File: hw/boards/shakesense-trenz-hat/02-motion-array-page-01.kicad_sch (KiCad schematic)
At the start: 12 parts, among them U11 LSM6DSOTR, U12 LSM6DSOTR, U13 LSM6DSOTR

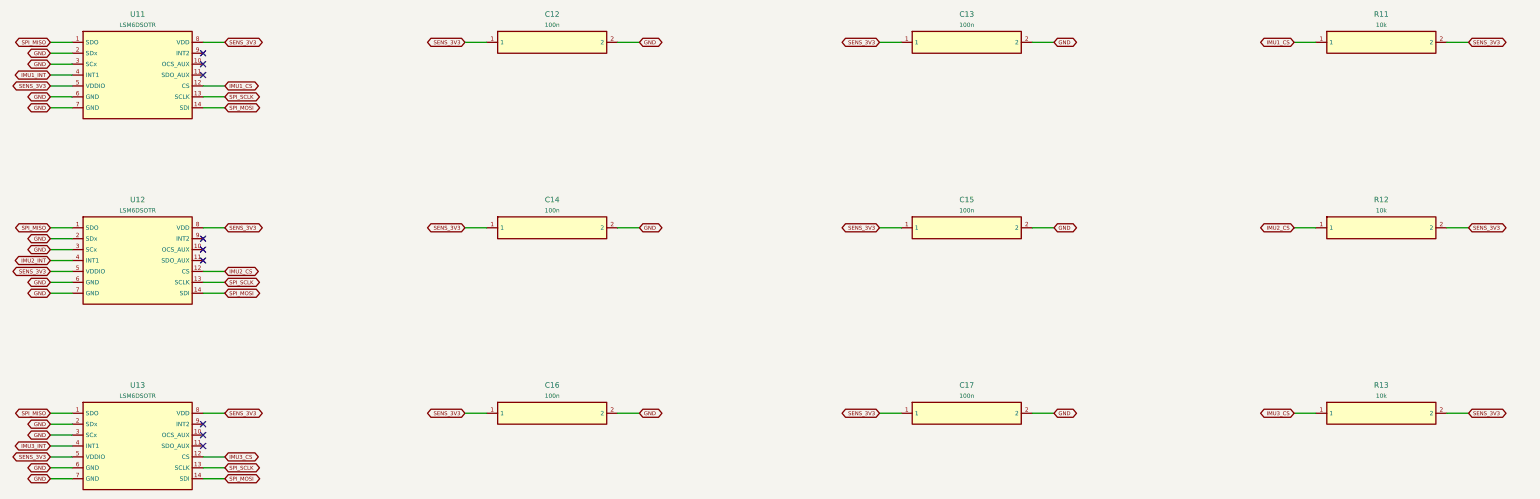
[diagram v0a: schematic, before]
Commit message: Expose Trenz GPIOs on the Pi-outline HDI sensor HAT
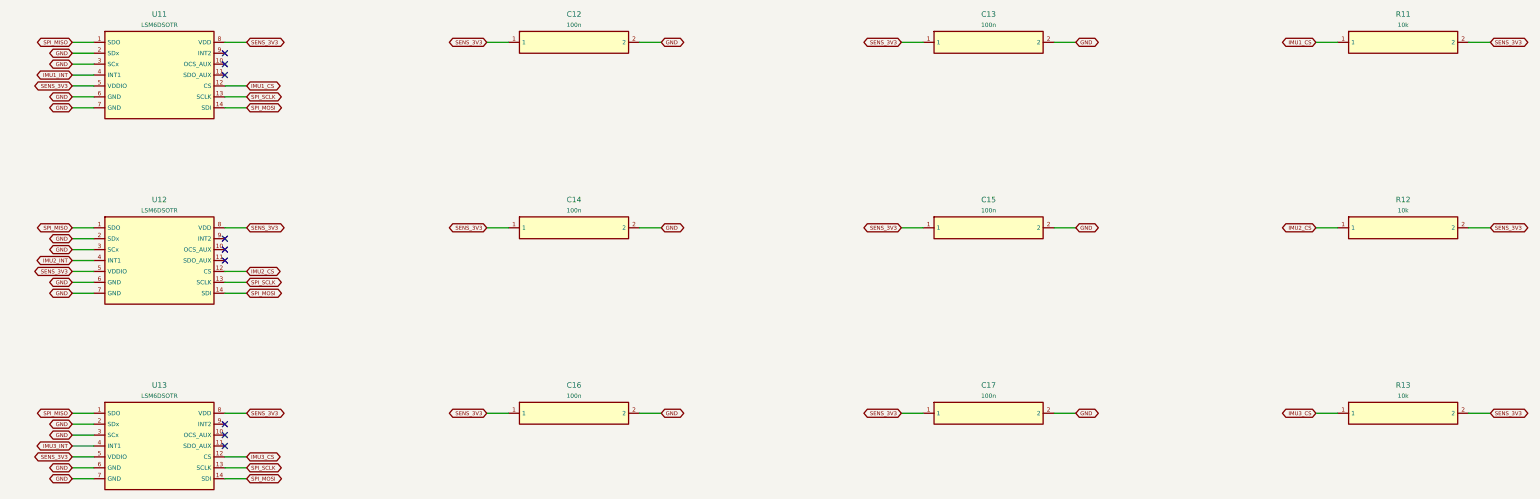
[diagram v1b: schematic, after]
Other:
- title: shakesense-trenz-hat / 02-motion-array-page-01 -> ShakeSense T1 / 02-motion-array-page-01
- moved on the sheet: C12, C13, C14, C15, C16, C17, R11, R12, R13, U11, U12, U13
